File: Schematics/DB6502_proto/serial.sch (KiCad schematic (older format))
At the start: 31 parts, among them J11 DB9_Male, U15 MAX232, U16 SC26C92, U17 FT230XS, U18 FT230XS, U4 74AC04, Y2 3,6864MHz

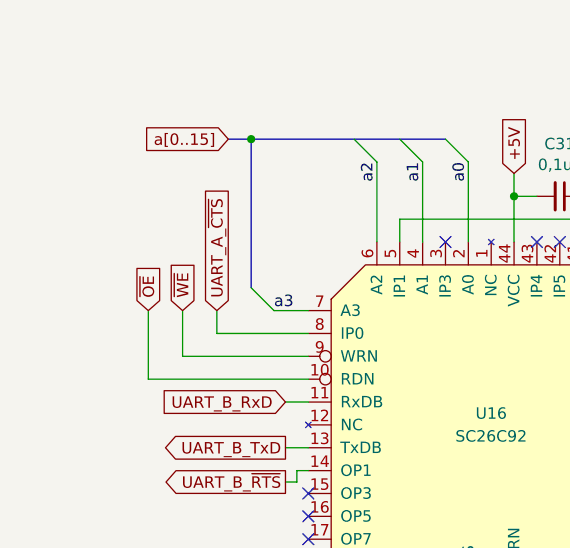
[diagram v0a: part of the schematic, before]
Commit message: Replaced nWE with nWR and nOE with nRD
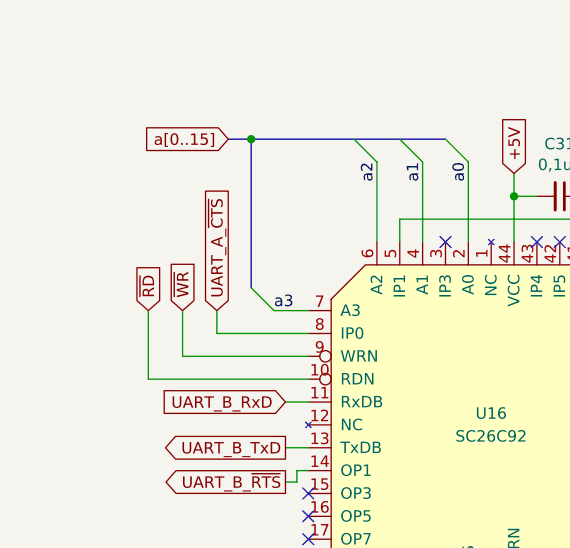
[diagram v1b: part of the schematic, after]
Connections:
- net labels added: ~RD, ~WR
- net labels removed: ~OE, ~WE
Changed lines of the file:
@@
 $EndComp
 Text GLabel 1050 1550 1    50   Input ~ 0
-~WE
+~WR
 Wire Wire Line
 	1050 1550 1050 1750
@@
 	1050 1750 1600 1750
 Text GLabel 900  1550 1    50   Input ~ 0
-~OE
+~RD
 Wire Wire Line
 	900  1550 900  1850

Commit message: Updated schematic to reflect new wait state generator design
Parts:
- renumbered C29 to C31, C30 to C32, C31 to C33, C32 to C34, C33 to C35, C34 to C36, C35 to C37, C36 to C38, C37 to C39, C38 to C40, C39 to C41, C40 to C42, R20 to R21, R21 to R22, R22 to R23, R23 to R24, U15 to U17, U16 to U18, U17 to U19, U18 to U20, U4 to U3
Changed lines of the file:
@@
 $Descr A4 11693 8268
 encoding utf-8
-Sheet 4 5
+Sheet 4 4
 Title "DB6502 Hobby Computer Version 2"
 Date "2020-11-03"
@@
 $EndDescr
 $Comp
-L 6502:SC26C92 U16
+L 6502:SC26C92 U18
 U 1 1 5F92CA23
 P 2400 2050
-F 0 "U16" H 2400 2100 50  0000 C CNN
+F 0 "U18" H 2400 2100 50  0000 C CNN
 F 1 "SC26C92" H 2400 2000 50  0000 C CNN
 F 2 "Package_LCC:PLCC-44_THT-Socket" H 2400 2050 50  0001 C CNN
@@
 	2500 950  2500 1050
 $Comp
-L Device:C_Small C31
+L Device:C_Small C33
 U 1 1 5F932BB1
 P 2700 1050
-F 0 "C31" V 2471 1050 50  0000 C CNN
+F 0 "C33" V 2471 1050 50  0000 C CNN
 F 1 "0,1uF" V 2562 1050 50  0000 C CNN
 F 2 "Capacitor_THT:C_Disc_D5.0mm_W2.5mm_P2.50mm" H 2700 1050 50  0001 C CNN
@@
 $EndComp
 $Comp
-L Device:C_Small C35
+L Device:C_Small C37
 U 1 1 5F93E98E
 P 3950 1500
-F 0 "C35" H 3858 1454 50  0000 R CNN
+F 0 "C37" H 3858 1454 50  0000 R CNN
 F 1 "22pF" H 3858 1545 50  0000 R CNN
 F 2 "Capacitor_THT:C_Disc_D5.0mm_W2.5mm_P2.50mm" H 3950 1500 50  0001 C CNN
@@
 $EndComp
 $Comp
-L Device:C_Small C36
+L Device:C_Small C38
 U 1 1 5F93F1BF
 P 3950 2100
-F 0 "C36" H 3858 2054 50  0000 R CNN
+F 0 "C38" H 3858 2054 50  0000 R CNN
 F 1 "22pF" H 3858 2145 50  0000 R CNN
 F 2 "Capacitor_THT:C_Disc_D5.0mm_W2.5mm_P2.50mm" H 3950 2100 50  0001 C CNN
@@
 AR Path="/6014B4D9/5F95BFD2" Ref="U?"  Part="1"
 AR Path="/5F8F4E1E/5F95BFD2" Ref="U?"  Part="1"
-AR Path="/5F910E81/5F95BFD2" Ref="U17"  Part="1"
-F 0 "U17" H 6350 2015 50  0000 C CNN
+AR Path="/5F910E81/5F95BFD2" Ref="U19"  Part="1"
+F 0 "U19" H 6350 2015 50  0000 C CNN
 F 1 "FT230XS" H 6350 1924 50  0000 C CNN
 F 2 "Package_SO:SSOP-16_5.3x6.2mm_P0.65mm" H 6350 1900 50  0001 C CNN
@@
 AR Path="/6014B4D9/5F95BFF2" Ref="C?"  Part="1"
 AR Path="/5F8F4E1E/5F95BFF2" Ref="C?"  Part="1"
-AR Path="/5F910E81/5F95BFF2" Ref="C37"  Part="1"
-F 0 "C37" H 5215 2296 50  0000 L CNN
+AR Path="/5F910E81/5F95BFF2" Ref="C39"  Part="1"
+F 0 "C39" H 5215 2296 50  0000 L CNN
 F 1 "0,1uF" H 5215 2205 50  0000 L CNN
 F 2 "Capacitor_THT:C_Disc_D5.0mm_W2.5mm_P2.50mm" H 5138 2100 50  0001 C CNN
@@
 AR Path="/6014B4D9/5F95C00C" Ref="R?"  Part="1"
 AR Path="/5F8F4E1E/5F95C00C" Ref="R?"  Part="1"
-AR Path="/5F910E81/5F95C00C" Ref="R20"  Part="1"
-F 0 "R20" V 6100 2250 50  0000 C CNN
+AR Path="/5F910E81/5F95C00C" Ref="R21"  Part="1"
+F 0 "R21" V 6100 2250 50  0000 C CNN
 F 1 "220" V 6000 2250 50  0000 C CNN
 F 2 "Resistor_THT:R_Axial_DIN0207_L6.3mm_D2.5mm_P10.16mm_Horizontal" V 5930 2250 50  0001 C CNN
@@
 P 7400 1350
 AR Path="/5F8F4E1E/5F95C03D" Ref="C?"  Part="1"
-AR Path="/5F910E81/5F95C03D" Ref="C38"  Part="1"
-F 0 "C38" H 7308 1304 50  0000 R CNN
+AR Path="/5F910E81/5F95C03D" Ref="C40"  Part="1"
+F 0 "C40" H 7308 1304 50  0000 R CNN
 F 1 "0,1uF" H 7308 1395 50  0000 R CNN
 F 2 "Capacitor_THT:C_Disc_D5.0mm_W2.5mm_P2.50mm" H 7400 1350 50  0001 C CNN
@@
 $Comp
 L 74xx:74LS04 U?
-U 6 1 5F9A15C7
+U 5 1 5F9A15C7
 P 1850 3850
 AR Path="/5F8F4E1E/5F9A15C7" Ref="U?"  Part="6"
-AR Path="/5F910E81/5F9A15C7" Ref="U4"  Part="6"
-F 0 "U4" H 1850 4167 50  0000 C CNN
+AR Path="/5F910E81/5F9A15C7" Ref="U3"  Part="5"
+F 0 "U3" H 1850 4167 50  0000 C CNN
 F 1 "74AC04" H 1850 4076 50  0000 C CNN
 F 2 "Package_DIP:DIP-14_W7.62mm_Socket" H 1850 3850 50  0001 C CNN
 F 3 "https://www.ti.com/lit/ds/symlink/sn74ac04.pdf" H 1850 3850 50  0001 C CNN
-	6    1850 3850
+	5    1850 3850
 	1    0    0    -1
 $EndComp
@@
 AR Path="/6014B4D9/5FA78290" Ref="R?"  Part="1"
 AR Path="/5F8F4E1E/5FA78290" Ref="R?"  Part="1"
-AR Path="/5F910E81/5FA78290" Ref="R21"  Part="1"
-F 0 "R21" V 6100 2550 50  0000 C CNN
+AR Path="/5F910E81/5FA78290" Ref="R22"  Part="1"
+F 0 "R22" V 6100 2550 50  0000 C CNN
 F 1 "220" V 6000 2550 50  0000 C CNN
 F 2 "Resistor_THT:R_Axial_DIN0207_L6.3mm_D2.5mm_P10.16mm_Horizontal" V 5930 2550 50  0001 C CNN
@@
 AR Path="/6014B4D9/5FF88878" Ref="U?"  Part="1"
 AR Path="/5F8F4E1E/5FF88878" Ref="U?"  Part="1"
-AR Path="/5F910E81/5FF88878" Ref="U18"  Part="1"
-F 0 "U18" H 9600 2015 50  0000 C CNN
+AR Path="/5F910E81/5FF88878" Ref="U20"  Part="1"
+F 0 "U20" H 9600 2015 50  0000 C CNN
 F 1 "FT230XS" H 9600 1924 50  0000 C CNN
 F 2 "Package_SO:SSOP-16_5.3x6.2mm_P0.65mm" H 9600 1900 50  0001 C CNN
@@
 AR Path="/6014B4D9/5FF88892" Ref="C?"  Part="1"
 AR Path="/5F8F4E1E/5FF88892" Ref="C?"  Part="1"
-AR Path="/5F910E81/5FF88892" Ref="C39"  Part="1"
-F 0 "C39" H 8465 2296 50  0000 L CNN
+AR Path="/5F910E81/5FF88892" Ref="C41"  Part="1"
+F 0 "C41" H 8465 2296 50  0000 L CNN
 F 1 "0,1uF" H 8465 2205 50  0000 L CNN
 F 2 "Capacitor_THT:C_Disc_D5.0mm_W2.5mm_P2.50mm" H 8388 2100 50  0001 C CNN
@@
 AR Path="/6014B4D9/5FF888A8" Ref="R?"  Part="1"
 AR Path="/5F8F4E1E/5FF888A8" Ref="R?"  Part="1"
-AR Path="/5F910E81/5FF888A8" Ref="R22"  Part="1"
-F 0 "R22" V 9350 2250 50  0000 C CNN
+AR Path="/5F910E81/5FF888A8" Ref="R23"  Part="1"
+F 0 "R23" V 9350 2250 50  0000 C CNN
 F 1 "220" V 9250 2250 50  0000 C CNN
 F 2 "Resistor_THT:R_Axial_DIN0207_L6.3mm_D2.5mm_P10.16mm_Horizontal" V 9180 2250 50  0001 C CNN
@@
 P 10650 1350
 AR Path="/5F8F4E1E/5FF888CE" Ref="C?"  Part="1"
-AR Path="/5F910E81/5FF888CE" Ref="C40"  Part="1"
-F 0 "C40" H 10558 1304 50  0000 R CNN
+AR Path="/5F910E81/5FF888CE" Ref="C42"  Part="1"
+F 0 "C42" H 10558 1304 50  0000 R CNN
 F 1 "0,1uF" H 10558 1395 50  0000 R CNN
 F 2 "Capacitor_THT:C_Disc_D5.0mm_W2.5mm_P2.50mm" H 10650 1350 50  0001 C CNN
@@
 AR Path="/6014B4D9/5FF8896B" Ref="R?"  Part="1"
 AR Path="/5F8F4E1E/5FF8896B" Ref="R?"  Part="1"
-AR Path="/5F910E81/5FF8896B" Ref="R23"  Part="1"
-F 0 "R23" V 9350 2550 50  0000 C CNN
+AR Path="/5F910E81/5FF8896B" Ref="R24"  Part="1"
+F 0 "R24" V 9350 2550 50  0000 C CNN
 F 1 "220" V 9250 2550 50  0000 C CNN
 F 2 "Resistor_THT:R_Axial_DIN0207_L6.3mm_D2.5mm_P10.16mm_Horizontal" V 9180 2550 50  0001 C CNN
@@
 GND
 $Comp
-L Device:CP_Small C30
+L Device:CP_Small C32
 U 1 1 5FB9DD34
 P 2400 5000
-F 0 "C30" V 2550 5000 50  0000 C CNN
+F 0 "C32" V 2550 5000 50  0000 C CNN
 F 1 "10uF" V 2250 5000 50  0000 C CNN
 F 2 "Capacitor_THT:CP_Radial_D4.0mm_P2.00mm" H 2400 5000 50  0001 C CNN
@@
 	3000 6200 3100 6200
 $Comp
-L Device:CP_Small C34
+L Device:CP_Small C36
 U 1 1 5FA4E5C0
 P 3200 6200
-F 0 "C34" V 3100 6100 50  0000 C CNN
+F 0 "C36" V 3100 6100 50  0000 C CNN
 F 1 "10uF" V 3100 6350 50  0000 C CNN
 F 2 "Capacitor_THT:CP_Radial_D4.0mm_P2.00mm" H 3200 6200 50  0001 C CNN
@@
 	3100 5900 3000 5900
 $Comp
-L Device:CP_Small C33
+L Device:CP_Small C35
 U 1 1 5FA453BA
 P 3200 5900
-F 0 "C33" V 3300 6000 50  0000 C CNN
+F 0 "C35" V 3300 6000 50  0000 C CNN
 F 1 "10uF" V 3300 5750 50  0000 C CNN
 F 2 "Capacitor_THT:CP_Radial_D4.0mm_P2.00mm" H 3200 5900 50  0001 C CNN
@@
 	3100 5650 3100 5700
 $Comp
-L Device:CP_Small C32
+L Device:CP_Small C34
 U 1 1 5FA2B0E8
 P 3100 5550
-F 0 "C32" H 3188 5596 50  0000 L CNN
+F 0 "C34" H 3188 5596 50  0000 L CNN
 F 1 "10uF" H 3188 5505 50  0000 L CNN
 F 2 "Capacitor_THT:CP_Radial_D4.0mm_P2.00mm" H 3100 5550 50  0001 C CNN
@@
 	1400 5700 1200 5700
 $Comp
-L Device:CP_Small C29
+L Device:CP_Small C31
 U 1 1 5FA0BA80
 P 1200 5550
-F 0 "C29" H 1288 5596 50  0000 L CNN
+F 0 "C31" H 1288 5596 50  0000 L CNN
 F 1 "10uF" H 1288 5505 50  0000 L CNN
 F 2 "Capacitor_THT:CP_Radial_D4.0mm_P2.00mm" H 1200 5550 50  0001 C CNN
@@
 +5V
 $Comp
-L Interface_UART:MAX232 U15
+L Interface_UART:MAX232 U17
 U 1 1 5F9EBE64
 P 2200 6300
-F 0 "U15" H 2200 6600 50  0000 C CNN
+F 0 "U17" H 2200 6600 50  0000 C CNN
 F 1 "MAX232" H 2200 6500 50  0000 C CNN
 F 2 "Package_DIP:DIP-16_W7.62mm_Socket" H 2250 5250 50  0001 L CNN

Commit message: Working on the second PCB
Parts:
- removed C31, C32, C34, C35, C36: 10uF, Capacitor_THT:CP_Radial_D4.0mm_P2.00mm, symbol Device:CP_Small
- removed C39, C40, C41, C42: 0,1uF, Capacitor_THT:C_Disc_D5.0mm_W2.5mm_P2.50mm, symbol Device:C_Small
- removed D5: A_RX, LED_THT:LED_D3.0mm, symbol Device:LED
- removed D6: B_TX, LED_THT:LED_D3.0mm, symbol Device:LED
- removed D7: B_RX, LED_THT:LED_D3.0mm, symbol Device:LED
- removed J11: DB9_Male, Connector_Dsub:DSUB-9_Male_Horizontal_P2.77x2.84mm_EdgePinOffset7.70mm_Housed_MountingHolesOffset9.12mm, symbol Connector:DB9_Male_MountingHoles
- removed JP2: UART B ~CTS~, Connector_PinHeader_2.54mm:PinHeader_1x02_P2.54mm_Vertical, symbol Jumper:Jumper_2_Open
- removed JP3: UART B RxD, Connector_PinHeader_2.54mm:PinHeader_1x02_P2.54mm_Vertical, symbol Jumper:Jumper_2_Open
- removed JP4: UART A ~CTS~, Connector_PinHeader_2.54mm:PinHeader_1x03_P2.54mm_Vertical, symbol Jumper:Jumper_3_Open
- removed JP5: UART A RxD, Connector_PinHeader_2.54mm:PinHeader_1x03_P2.54mm_Vertical, symbol Jumper:Jumper_3_Open
- removed R21, R22, R23, R24: 220, Resistor_THT:R_Axial_DIN0207_L6.3mm_D2.5mm_P10.16mm_Horizontal, symbol Device:R
- removed U17: MAX232, Package_DIP:DIP-16_W7.62mm_Socket, symbol Interface_UART:MAX232
- removed U19, U20: FT230XS, Package_SO:SSOP-16_5.3x6.2mm_P0.65mm, symbol 6502:FT230XS
- added C30: 0,1uF, Capacitor_SMD:C_0805_2012Metric_Pad1.15x1.40mm_HandSolder, symbol Device:C_Small
- added J10: LCD Port, Connector_PinSocket_2.54mm:PinSocket_1x16_P2.54mm_Vertical, symbol Connector:Conn_01x16_Female
- added J11: VIA Ports, Connector_PinSocket_2.54mm:PinSocket_1x20_P2.54mm_Vertical, symbol Connector:Conn_01x20_Female
- added JP10: Blink, Connector_PinHeader_2.54mm:PinHeader_2x01_P2.54mm_Vertical, symbol Jumper:Jumper_2_Open
- added R18: 0R, Resistor_THT:R_Axial_DIN0207_L6.3mm_D2.5mm_P10.16mm_Horizontal, symbol Device:R
- added R19: 220, Resistor_THT:R_Axial_DIN0207_L6.3mm_D2.5mm_P10.16mm_Horizontal, symbol Device:R
- added RV1: 10K, Potentiometer_THT:Potentiometer_Piher_PT-10-V10_Vertical, symbol Device:R_POT
- added U19: 65C22S, Package_DIP:DIP-40_W15.24mm_Socket, symbol 6502:65C22S
- C27: renamed from C33; footprint Capacitor_THT:C_Disc_D5.0mm_W2.5mm_P2.50mm -> Capacitor_SMD:C_0805_2012Metric_Pad1.15x1.40mm_HandSolder
- D4: value A_TX -> BLINK
- renumbered C37 to C28, C38 to C29, U3 to U8
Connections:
- net labels added: 6502_CLK, IOCS, R~W, v1pa0, v1pa1, v1pa2, v1pa3, v1pa4, v1pa5, v1pa6, v1pa7, v1pa8, v1pa9, v1pb0, v1pb1, v1pb2, v1pb3, v1pb4, v1pb5, v1pb6, v1pb7, v1pb8, v1pb9, ~VIA1, ~VIA1_IRQ
- net labels removed: 232_RxD, 232_TxD, 232_~CTS, 232_~RTS, UART_A_RxD_232, UART_A_RxD_USB, UART_A_USBD+, UART_A_USBD-, UART_A_~CTS~_232, UART_A_~CTS~_USB, UART_B_RxD_USB, UART_B_USBD+, UART_B_USBD-, UART_B_~CTS~_USB, ~UART_A_RXLED, ~UART_A_TXLED, ~UART_B_RXLED, ~UART_B_TXLED
- wire segments 207 -> 163
- no-connect marks 17 -> 11

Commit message: Working on a PCB - first traces routed
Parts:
- U8: footprint Package_DIP:DIP-14_W7.62mm_Socket -> Package_SO:SOIC-14_3.9x8.7mm_P1.27mm
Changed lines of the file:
@@
 F 0 "U8" H 1850 4167 50  0000 C CNN
 F 1 "74AC04" H 1850 4076 50  0000 C CNN
-F 2 "Package_DIP:DIP-14_W7.62mm_Socket" H 1850 3850 50  0001 C CNN
+F 2 "Package_SO:SOIC-14_3.9x8.7mm_P1.27mm" H 1850 3850 50  0001 C CNN
 F 3 "https://www.ti.com/lit/ds/symlink/sn74ac04.pdf" H 1850 3850 50  0001 C CNN
 	5    1850 3850

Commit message: Increased capacitor footprints to 1206
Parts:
- C27, C30: footprint Capacitor_SMD:C_0805_2012Metric_Pad1.15x1.40mm_HandSolder -> Capacitor_SMD:C_1206_3216Metric_Pad1.42x1.75mm_HandSolder
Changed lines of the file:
@@
 F 0 "C27" V 2471 1050 50  0000 C CNN
 F 1 "0,1uF" V 2562 1050 50  0000 C CNN
-F 2 "Capacitor_SMD:C_0805_2012Metric_Pad1.15x1.40mm_HandSolder" H 2700 1050 50  0001 C CNN
+F 2 "Capacitor_SMD:C_1206_3216Metric_Pad1.42x1.75mm_HandSolder" H 2700 1050 50  0001 C CNN
 F 3 "~" H 2700 1050 50  0001 C CNN
 	1    2700 1050
@@
 F 0 "C30" V 5571 3500 50  0000 C CNN
 F 1 "0,1uF" V 5662 3500 50  0000 C CNN
-F 2 "Capacitor_SMD:C_0805_2012Metric_Pad1.15x1.40mm_HandSolder" H 5800 3500 50  0001 C CNN
+F 2 "Capacitor_SMD:C_1206_3216Metric_Pad1.42x1.75mm_HandSolder" H 5800 3500 50  0001 C CNN
 F 3 "~" H 5800 3500 50  0001 C CNN
 	1    5800 3500
